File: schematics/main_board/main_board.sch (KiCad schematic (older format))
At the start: 24 parts, among them J1 USB_B_Micro, U1 STM32F405RGTx, X1 Resonator 8MHz

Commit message: Added motors, voltage regulator and LED's
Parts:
- added BT1: Battery_Cell, Battery:BatteryHolder_Keystone_1042_1x18650, symbol Device:Battery_Cell
- added C3, C4: 10uF, symbol Device:C
- added D1: BAT54C, Package_TO_SOT_SMD:SOT-23, symbol Diode:BAT54C
- added D2, D3: LED, symbol Device:LED
- added D4, D5, D6, D7: D_Schottky, symbol Device:D_Schottky
- added M1, M2, M3, M4: Motor_DC, symbol Motor:Motor_DC
- added Q1: BC817, Package_TO_SOT_SMD:SOT-23, symbol Transistor_BJT:BC817
- added Q2, Q3, Q4, Q5: 2N7002, Package_TO_SOT_SMD:SOT-23, symbol Transistor_FET:2N7002
- added R10, R13, R14, R9: 10K, symbol Device:R
- added R11, R12, R7, R8: 100, symbol Device:R
- added R3, R4: R, symbol Device:R
- added R5, R6: 1K, symbol Device:R
- added U2: NCP1117-1.5_SOT223, Package_TO_SOT_SMD:SOT-223-3_TabPin2, symbol Regulator_Linear:NCP1117-1.5_SOT223
- gave numbers to parts that had none: 13
- renumbered R1_USB to R1_USB1, R2_G to R2_G1, R2_USB to R2_USB1, R_BOOT to R_BOOT1
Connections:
- net 5V_USB: now also D1.1
- net GND: now also BT1.2 (-), C3.2, C4.2, D2.1 (K), D3.1 (K), Q1.2 (E), Q2.2 (S), Q3.2 (S), Q4.2 (S), Q5.2 (S), R10.1, R13.1, R14.1, R9.1, U2.1 (GND)
- net LED1: now also R5.1
- net LED2: now also R6.2
- net S2: now also R8.2
- net S3: now also R11.2
- net UART1_RX: now also Q1.3 (C), R4.2
- net VBAT_PAD: now also BT1.1 (+), D4.1 (K), D5.1 (K), D6.1 (K), D7.1 (K), M1.1 (+), M2.1 (+), M3.1 (+), M4.1 (+)
- net VCC: now also C4.1, U2.2 (VO)
- new net: C3.1, D1.3, U2.3 (VI)
- new net: Q1.1 (B), R3.1
- new net: D2.2 (A), R5.2
- new net: D3.2 (A), R6.1
- new net: D4.2 (A), Q2.1 (G), R7.1, R9.2
- new net: M1.2 (-), Q2.3 (D)
- new net: D6.2 (A), Q4.1 (G), R11.1, R13.2
- new net: M3.2 (-), Q4.3 (D)
- new net: D5.2 (A), Q3.1 (G), R10.2, R8.1
- new net: M2.2 (-), Q3.3 (D)
- new net: D7.2 (A), Q5.1 (G), R12.1, R14.2
- new net: M4.2 (-), Q5.3 (D)
- new net 5V_EXTERNAL: D1.2, R4.1
- new net S1: R7.2
- new net S4: R12.2
- new net SBUS: R3.2

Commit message: Created the PCB frame and added the components on top
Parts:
- C1, C10, C11, C12, C13, C2, C3, C4, C5, C6, C7, C8, C9: footprint (none) -> Capacitor_SMD:C_0402_1005Metric
- D2, D3: footprint (none) -> LED_SMD:LED_0402_1005Metric
- D4, D5, D6, D7: footprint (none) -> Diode_SMD:D_01005_0402Metric
- J1: footprint (none) -> Connector_USB:USB_Micro-B_Molex-105133-0031
- M1, M2, M3, M4: footprint (none) -> TerminalBlock:TerminalBlock_Altech_AK300-2_P5.00mm
- R1, R10, R11, R12, R13, R14, R15, R16, R1_USB1, R2, R2_G1, R2_USB1, R3, R4, R5, R6, R7, R8, R9, R_BOOT1: footprint (none) -> Resistor_SMD:R_0402_1005Metric
- SW1: footprint (none) -> Button_Switch_SMD:SW_SPST_REED_CT05-XXXX-J1
- X1: footprint (none) -> Crystal:Resonator_SMD_muRata_CSTxExxV-3Pin_3.0x1.1mm_HandSoldering

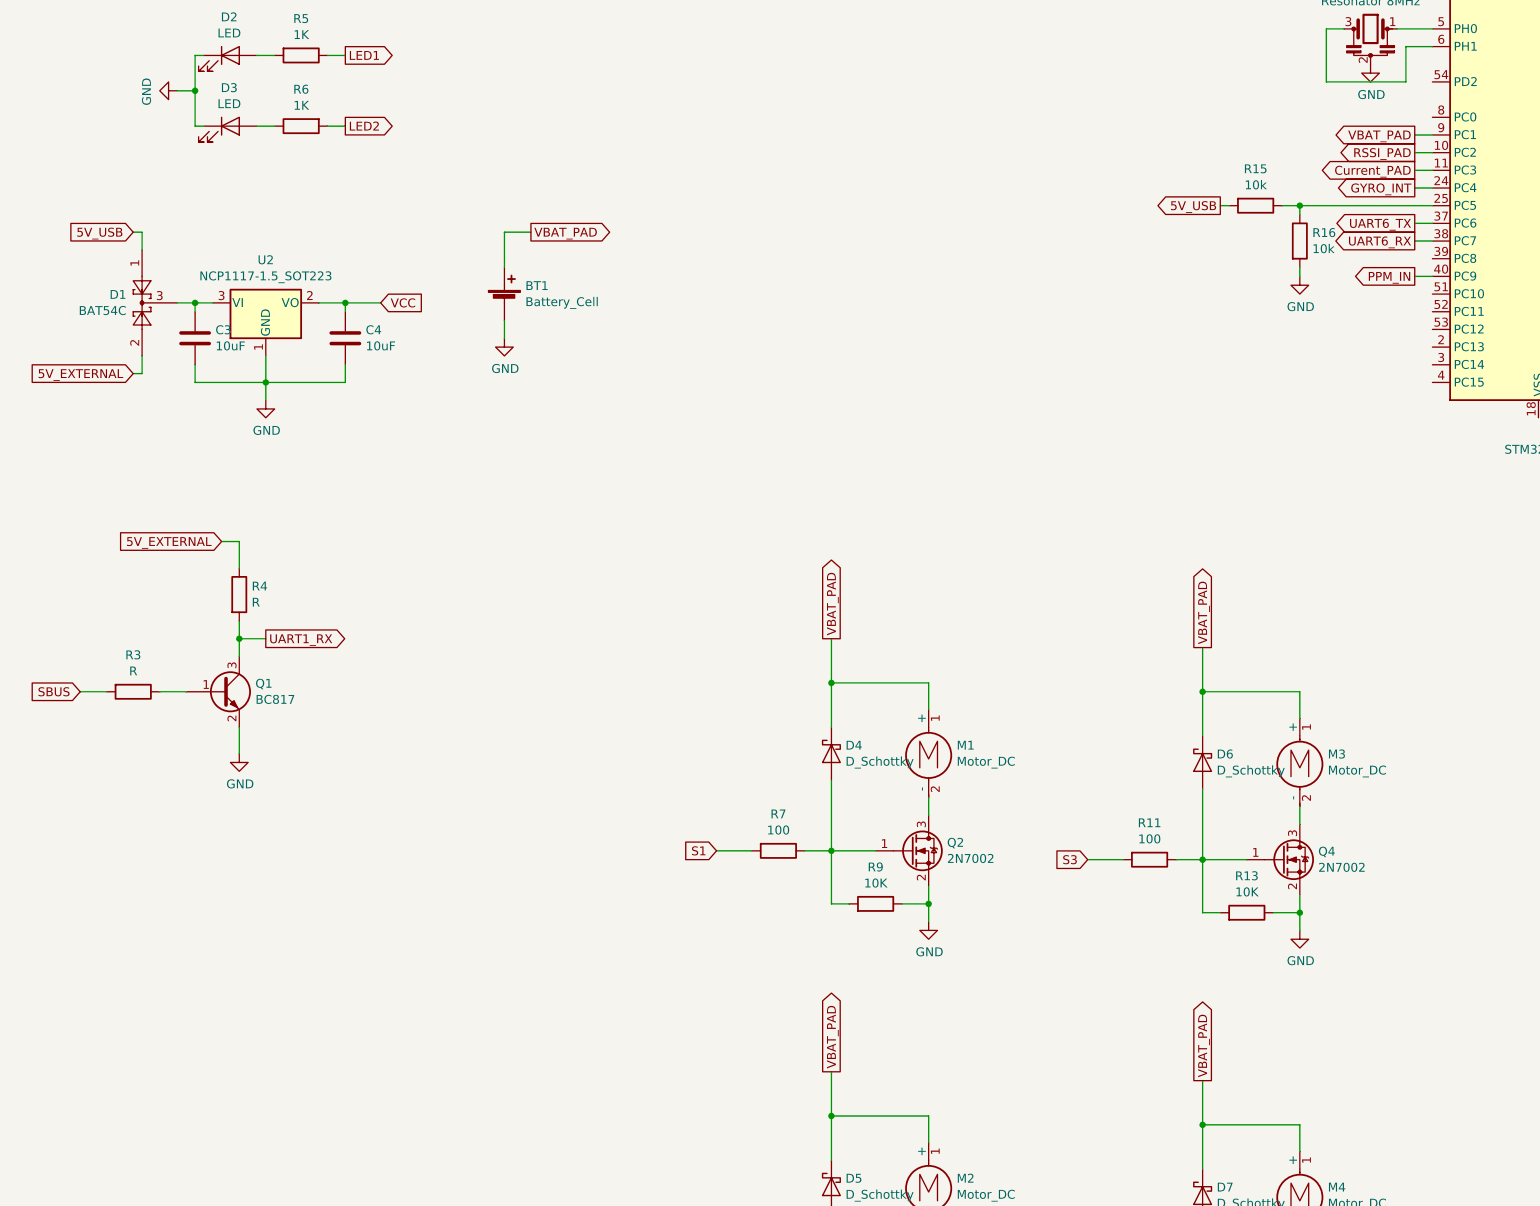
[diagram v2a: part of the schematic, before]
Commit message: Changed some footprints, added some traces
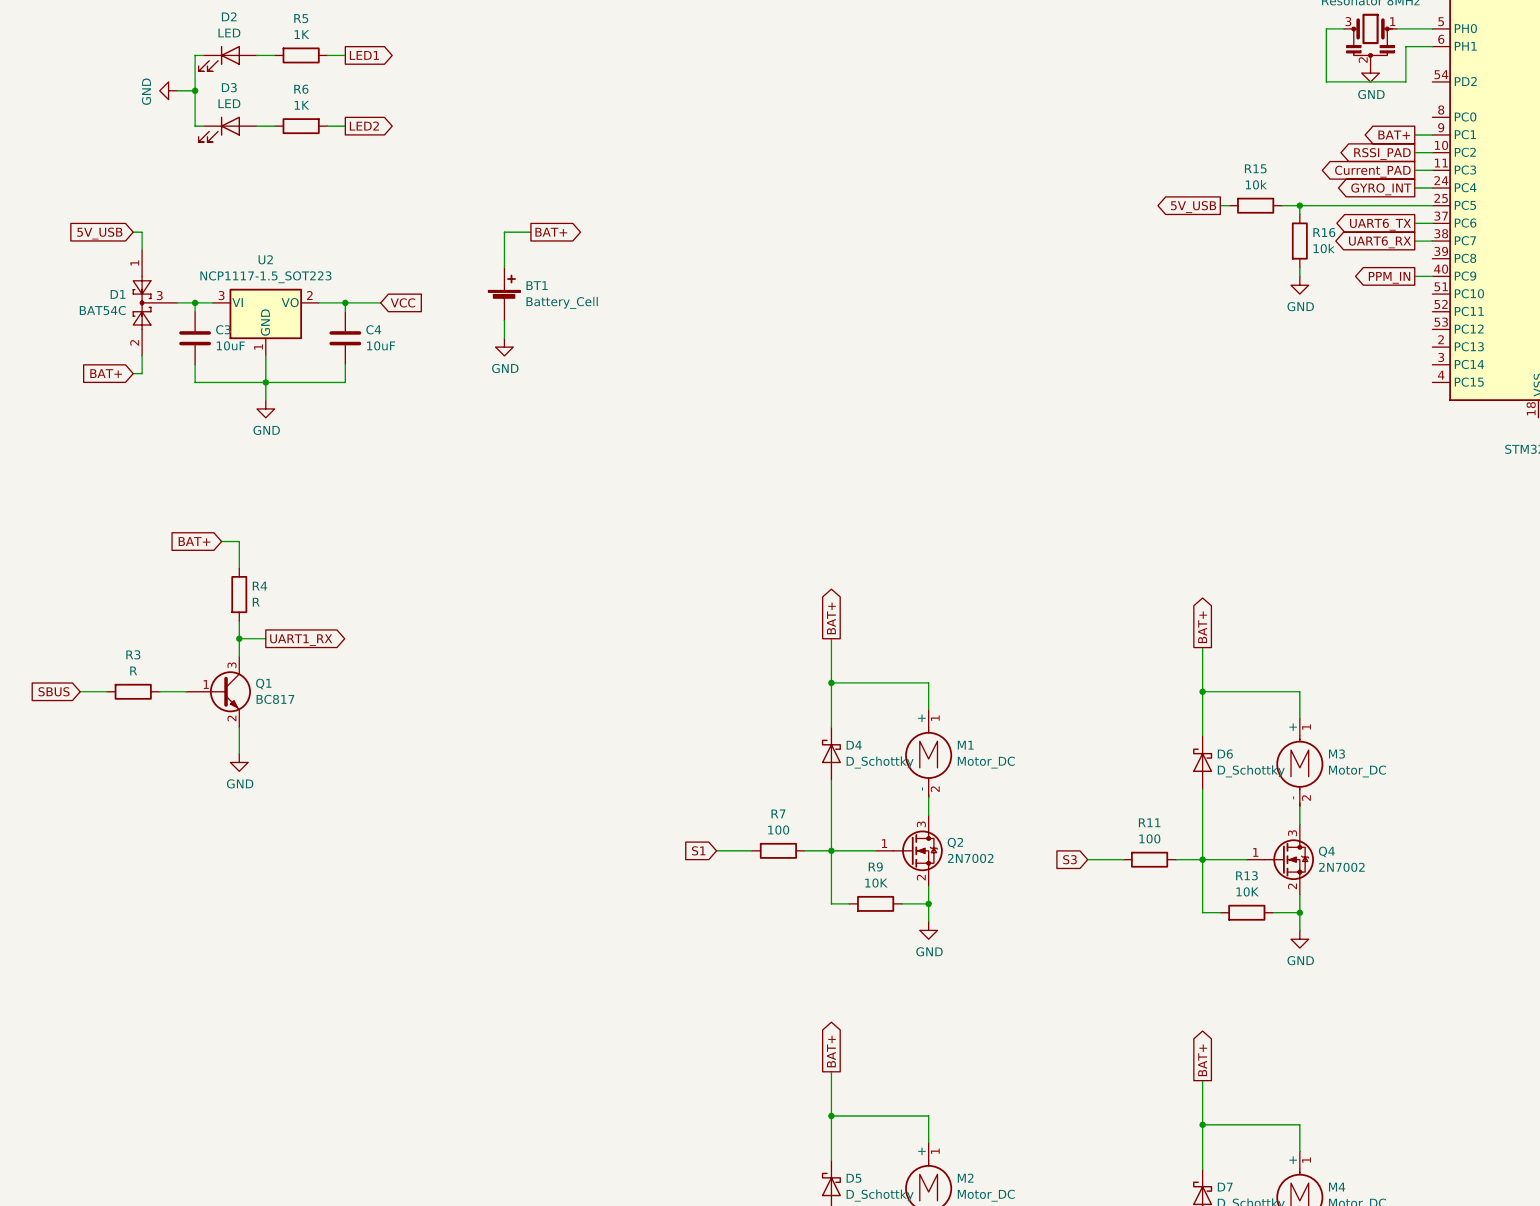
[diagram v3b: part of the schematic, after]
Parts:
- C1, C10, C11, C12, C13, C2, C3, C4, C5, C6, C7, C8, C9: footprint Capacitor_SMD:C_0402_1005Metric -> Capacitor_SMD:C_0805_2012Metric
- D1: footprint Package_TO_SOT_SMD:SOT-23 -> Diode_SMD:D_SOT-23_ANK
- D2, D3: footprint LED_SMD:LED_0402_1005Metric -> LED_SMD:LED_0805_2012Metric
- D4, D5, D6, D7: footprint Diode_SMD:D_01005_0402Metric -> Diode_SMD:D_0805_2012Metric
- M1, M2, M3, M4: footprint TerminalBlock:TerminalBlock_Altech_AK300-2_P5.00mm -> Buzzer_Beeper:Buzzer_CUI_CPT-9019S-SMT
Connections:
- net VBAT_PAD is gone; now on net BAT+: BT1.1 (+), D4.1 (K), D5.1 (K), D6.1 (K), D7.1 (K), M1.1 (+), M2.1 (+), M3.1 (+), M4.1 (+), U1.9 (PC1)
- net 5V_EXTERNAL renamed BAT+
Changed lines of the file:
@@
 F 0 "C2" H 8686 2504 50  0000 R CNN
 F 1 "100nF" H 8686 2595 50  0000 R CNN
-F 2 "Capacitor_SMD:C_0402_1005Metric" H 8838 2400 50  0001 C CNN
+F 2 "Capacitor_SMD:C_0805_2012Metric" H 8838 2400 50  0001 C CNN
 F 3 "~" H 8800 2550 50  0001 C CNN
 	1    8800 2550
@@
 F 0 "C1" H 8236 2504 50  0000 R CNN
 F 1 "100nF" H 8236 2595 50  0000 R CNN
-F 2 "Capacitor_SMD:C_0402_1005Metric" H 8388 2400 50  0001 C CNN
+F 2 "Capacitor_SMD:C_0805_2012Metric" H 8388 2400 50  0001 C CNN
 F 3 "~" H 8350 2550 50  0001 C CNN
 	1    8350 2550
@@
 	8300 3100 8300 3400
 Text GLabel 8800 3700 0    50   Output ~ 0
-VBAT_PAD
+BAT+
 Text GLabel 8800 3800 0    50   Output ~ 0
 RSSI_PAD
@@
 F 0 "C5" H 9509 1304 50  0000 R CNN
 F 1 "100nF" H 9509 1395 50  0000 R CNN
-F 2 "Capacitor_SMD:C_0402_1005Metric" H 9600 1350 50  0001 C CNN
+F 2 "Capacitor_SMD:C_0805_2012Metric" H 9600 1350 50  0001 C CNN
 F 3 "~" H 9600 1350 50  0001 C CNN
 	1    9600 1350
@@
 F 0 "C6" H 9609 1104 50  0001 R CNN
 F 1 "100nF" H 9609 1195 50  0001 R CNN
-F 2 "Capacitor_SMD:C_0402_1005Metric" H 9700 1150 50  0001 C CNN
+F 2 "Capacitor_SMD:C_0805_2012Metric" H 9700 1150 50  0001 C CNN
 F 3 "~" H 9700 1150 50  0001 C CNN
 	1    9700 1150
@@
 F 0 "C7" H 9709 1304 50  0001 R CNN
 F 1 "100nF" H 9709 1395 50  0001 R CNN
-F 2 "Capacitor_SMD:C_0402_1005Metric" H 9800 1350 50  0001 C CNN
+F 2 "Capacitor_SMD:C_0805_2012Metric" H 9800 1350 50  0001 C CNN
 F 3 "~" H 9800 1350 50  0001 C CNN
 	1    9800 1350
@@
 F 0 "C8" H 9809 1104 50  0001 R CNN
 F 1 "100nF" H 9809 1195 50  0001 R CNN
-F 2 "Capacitor_SMD:C_0402_1005Metric" H 9900 1150 50  0001 C CNN
+F 2 "Capacitor_SMD:C_0805_2012Metric" H 9900 1150 50  0001 C CNN
 F 3 "~" H 9900 1150 50  0001 C CNN
 	1    9900 1150
@@
 F 0 "C9" H 9909 1304 50  0001 R CNN
 F 1 "100nF" H 9909 1395 50  0001 R CNN
-F 2 "Capacitor_SMD:C_0402_1005Metric" H 10000 1350 50  0001 C CNN
+F 2 "Capacitor_SMD:C_0805_2012Metric" H 10000 1350 50  0001 C CNN
 F 3 "~" H 10000 1350 50  0001 C CNN
 	1    10000 1350
@@
 F 0 "C13" V 14871 2450 50  0000 C CNN
 F 1 "2.2nF" V 14962 2450 50  0000 C CNN
-F 2 "Capacitor_SMD:C_0402_1005Metric" H 15100 2450 50  0001 C CNN
+F 2 "Capacitor_SMD:C_0805_2012Metric" H 15100 2450 50  0001 C CNN
 F 3 "~" H 15100 2450 50  0001 C CNN
 	1    15100 2450
@@
 F 0 "C11" V 13621 1300 50  0000 C CNN
 F 1 "0.1uF" V 13712 1300 50  0000 C CNN
-F 2 "Capacitor_SMD:C_0402_1005Metric" H 13850 1300 50  0001 C CNN
+F 2 "Capacitor_SMD:C_0805_2012Metric" H 13850 1300 50  0001 C CNN
 F 3 "~" H 13850 1300 50  0001 C CNN
 	1    13850 1300
@@
 F 0 "C10" V 13271 1300 50  0000 C CNN
 F 1 "1uF" V 13362 1300 50  0000 C CNN
-F 2 "Capacitor_SMD:C_0402_1005Metric" H 13500 1300 50  0001 C CNN
+F 2 "Capacitor_SMD:C_0805_2012Metric" H 13500 1300 50  0001 C CNN
 F 3 "~" H 13500 1300 50  0001 C CNN
 	1    13500 1300
@@
 F 0 "C12" H 14808 2654 50  0000 R CNN
 F 1 "0.1uF" H 14808 2745 50  0000 R CNN
-F 2 "Capacitor_SMD:C_0402_1005Metric" H 14900 2700 50  0001 C CNN
+F 2 "Capacitor_SMD:C_0805_2012Metric" H 14900 2700 50  0001 C CNN
 F 3 "~" H 14900 2700 50  0001 C CNN
 	1    14900 2700
@@
 F 0 "D1" V 1554 4738 50  0000 L CNN
 F 1 "BAT54C" V 1645 4738 50  0000 L CNN
-F 2 "Package_TO_SOT_SMD:SOT-23" H 1675 4775 50  0001 L CNN
+F 2 "Diode_SMD:D_SOT-23_ANK" H 1675 4775 50  0001 L CNN
 F 3 "http://www.diodes.com/_files/datasheets/ds11005.pdf" H 1520 4650 50  0001 C CNN
 	1    1600 4650
@@
 5V_USB
 Text GLabel 1550 5050 0    50   Input ~ 0
-5V_EXTERNAL
+BAT+
 Wire Wire Line
 	1550 4250 1600 4250
@@
 F 0 "C3" H 2015 4896 50  0000 L CNN
 F 1 "10uF" H 2015 4805 50  0000 L CNN
-F 2 "Capacitor_SMD:C_0402_1005Metric" H 1938 4700 50  0001 C CNN
+F 2 "Capacitor_SMD:C_0805_2012Metric" H 1938 4700 50  0001 C CNN
 F 3 "~" H 1900 4850 50  0001 C CNN
 	1    1900 4850
@@
 F 0 "C4" H 2865 4896 50  0000 L CNN
 F 1 "10uF" H 2865 4805 50  0000 L CNN
-F 2 "Capacitor_SMD:C_0402_1005Metric" H 2788 4700 50  0001 C CNN
+F 2 "Capacitor_SMD:C_0805_2012Metric" H 2788 4700 50  0001 C CNN
 F 3 "~" H 2750 4850 50  0001 C CNN
 	1    2750 4850
@@
 $EndComp
 Text GLabel 2050 6000 0    50   Input ~ 0
-5V_EXTERNAL
+BAT+
 Text GLabel 2300 6550 2    50   Output ~ 0
 UART1_RX
@@
 F 0 "D2" H 2093 3466 50  0000 C CNN
 F 1 "LED" H 2093 3375 50  0000 C CNN
-F 2 "LED_SMD:LED_0402_1005Metric" H 2100 3250 50  0001 C CNN
+F 2 "LED_SMD:LED_0805_2012Metric" H 2100 3250 50  0001 C CNN
 F 3 "~" H 2100 3250 50  0001 C CNN
 	1    2100 3250
@@
 F 0 "D3" H 2093 3866 50  0000 C CNN
 F 1 "LED" H 2093 3775 50  0000 C CNN
-F 2 "LED_SMD:LED_0402_1005Metric" H 2100 3650 50  0001 C CNN
+F 2 "LED_SMD:LED_0805_2012Metric" H 2100 3650 50  0001 C CNN
 F 3 "~" H 2100 3650 50  0001 C CNN
 	1    2100 3650
@@
 F 0 "D4" V 5454 7121 50  0000 R CNN
 F 1 "D_Schottky" V 5545 7121 50  0000 R CNN
-F 2 "Diode_SMD:D_01005_0402Metric" H 5500 7200 50  0001 C CNN
+F 2 "Diode_SMD:D_0805_2012Metric" H 5500 7200 50  0001 C CNN
 F 3 "~" H 5500 7200 50  0001 C CNN
 	1    5500 7200
@@
 F 0 "M1" H 6208 7146 50  0000 L CNN
 F 1 "Motor_DC" H 6208 7055 50  0000 L CNN
-F 2 "TerminalBlock:TerminalBlock_Altech_AK300-2_P5.00mm" H 6050 7060 50  0001 C CNN
+F 2 "Buzzer_Beeper:Buzzer_CUI_CPT-9019S-SMT" H 6050 7060 50  0001 C CNN
 F 3 "~" H 6050 7060 50  0001 C CNN
 	1    6050 7150
@@
 $EndComp
 Text GLabel 3800 4250 2    50   Output ~ 0
-VBAT_PAD
+BAT+
 Wire Wire Line
 	3650 4450 3650 4250
@@
 	3650 4850 3650 4750
 Text GLabel 5500 6550 1    50   Output ~ 0
-VBAT_PAD
+BAT+
 $Comp
 L Device:R R9
@@
 F 0 "D6" V 7554 7171 50  0000 R CNN
 F 1 "D_Schottky" V 7645 7171 50  0000 R CNN
-F 2 "Diode_SMD:D_01005_0402Metric" H 7600 7250 50  0001 C CNN
+F 2 "Diode_SMD:D_0805_2012Metric" H 7600 7250 50  0001 C CNN
 F 3 "~" H 7600 7250 50  0001 C CNN
 	1    7600 7250
@@
 F 0 "M3" H 8308 7196 50  0000 L CNN
 F 1 "Motor_DC" H 8308 7105 50  0000 L CNN
-F 2 "TerminalBlock:TerminalBlock_Altech_AK300-2_P5.00mm" H 8150 7110 50  0001 C CNN
+F 2 "Buzzer_Beeper:Buzzer_CUI_CPT-9019S-SMT" H 8150 7110 50  0001 C CNN
 F 3 "~" H 8150 7110 50  0001 C CNN
 	1    8150 7200
@@
 $EndComp
 Text GLabel 7600 6600 1    50   Output ~ 0
-VBAT_PAD
+BAT+
 $Comp
 L Device:R R13
@@
 F 0 "D5" V 5454 9571 50  0000 R CNN
 F 1 "D_Schottky" V 5545 9571 50  0000 R CNN
-F 2 "Diode_SMD:D_01005_0402Metric" H 5500 9650 50  0001 C CNN
+F 2 "Diode_SMD:D_0805_2012Metric" H 5500 9650 50  0001 C CNN
 F 3 "~" H 5500 9650 50  0001 C CNN
 	1    5500 9650
@@
 F 0 "M2" H 6208 9596 50  0000 L CNN
 F 1 "Motor_DC" H 6208 9505 50  0000 L CNN
-F 2 "TerminalBlock:TerminalBlock_Altech_AK300-2_P5.00mm" H 6050 9510 50  0001 C CNN
+F 2 "Buzzer_Beeper:Buzzer_CUI_CPT-9019S-SMT" H 6050 9510 50  0001 C CNN
 F 3 "~" H 6050 9510 50  0001 C CNN
 	1    6050 9600
@@
 $EndComp
 Text GLabel 5500 9000 1    50   Output ~ 0
-VBAT_PAD
+BAT+
 $Comp
 L Device:R R10
@@
 F 0 "D7" V 7554 9621 50  0000 R CNN
 F 1 "D_Schottky" V 7645 9621 50  0000 R CNN
-F 2 "Diode_SMD:D_01005_0402Metric" H 7600 9700 50  0001 C CNN
+F 2 "Diode_SMD:D_0805_2012Metric" H 7600 9700 50  0001 C CNN
 F 3 "~" H 7600 9700 50  0001 C CNN
 	1    7600 9700
@@
 F 0 "M4" H 8308 9646 50  0000 L CNN
 F 1 "Motor_DC" H 8308 9555 50  0000 L CNN
-F 2 "TerminalBlock:TerminalBlock_Altech_AK300-2_P5.00mm" H 8150 9560 50  0001 C CNN
+F 2 "Buzzer_Beeper:Buzzer_CUI_CPT-9019S-SMT" H 8150 9560 50  0001 C CNN
 F 3 "~" H 8150 9560 50  0001 C CNN
 	1    8150 9650
@@
 $EndComp
 Text GLabel 7600 9050 1    50   Output ~ 0
-VBAT_PAD
+BAT+
 $Comp
 L Device:R R14

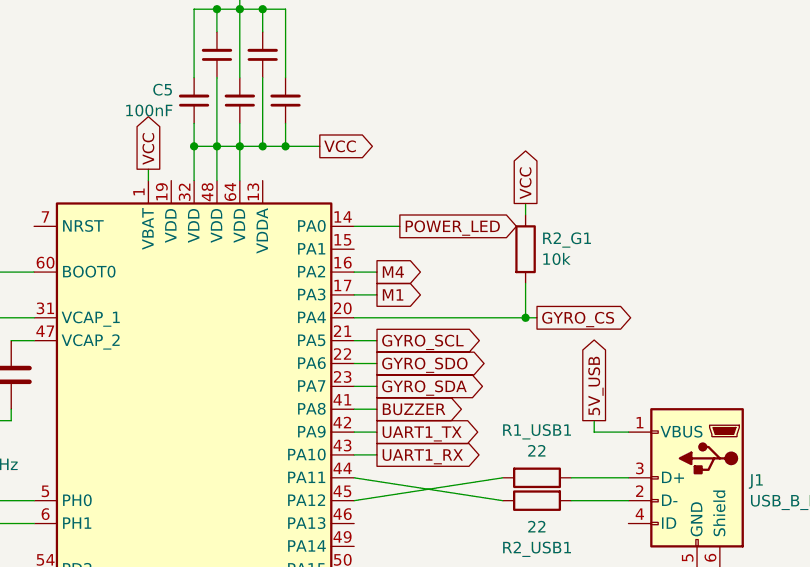
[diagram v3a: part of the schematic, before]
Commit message: Fixed oscillator footprint and motor signal names
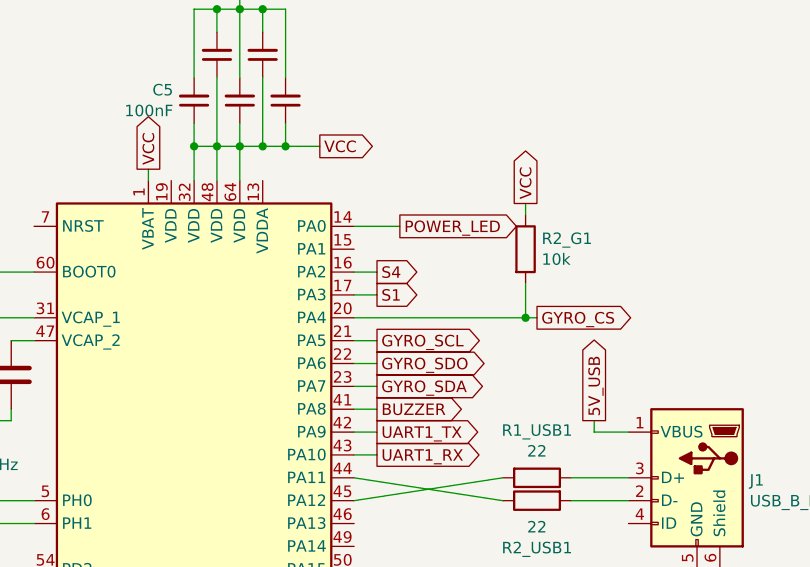
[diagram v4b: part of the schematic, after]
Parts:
- D1: footprint Diode_SMD:D_SOT-23_ANK -> Package_TO_SOT_SMD:SOT-23
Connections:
- net M1 is gone; now on net S1: U1.17 (PA3)
- net M4 is gone; now on net S4: U1.16 (PA2)
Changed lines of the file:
@@
 	10300 1900 10500 1900
 Text GLabel 10400 2100 2    50   Output ~ 0
-M4
+S4
 Text GLabel 10400 2200 2    50   Output ~ 0
-M1
+S1
 $Comp
 L Sensor_Motion:MPU-6000 U3
@@
 F 0 "D1" V 1554 4738 50  0000 L CNN
 F 1 "BAT54C" V 1645 4738 50  0000 L CNN
-F 2 "Diode_SMD:D_SOT-23_ANK" H 1675 4775 50  0001 L CNN
+F 2 "Package_TO_SOT_SMD:SOT-23" H 1675 4775 50  0001 L CNN
 F 3 "http://www.diodes.com/_files/datasheets/ds11005.pdf" H 1520 4650 50  0001 C CNN
 	1    1600 4650
